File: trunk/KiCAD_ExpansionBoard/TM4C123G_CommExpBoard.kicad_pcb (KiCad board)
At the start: 2 copper layers, 50.8 x 58.4 mm, 58 parts, among them J1 TI_BOOSTER_40_J1, J2 TI_BOOSTER_40_J2, J3 TI_BOOSTER_40_J3, J4 TI_BOOSTER_40_J4, P1 ANT_GND, P10 EB_GPIO0, P5 ANT_C, P6 CAN, P7 UART1, P8 RS485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

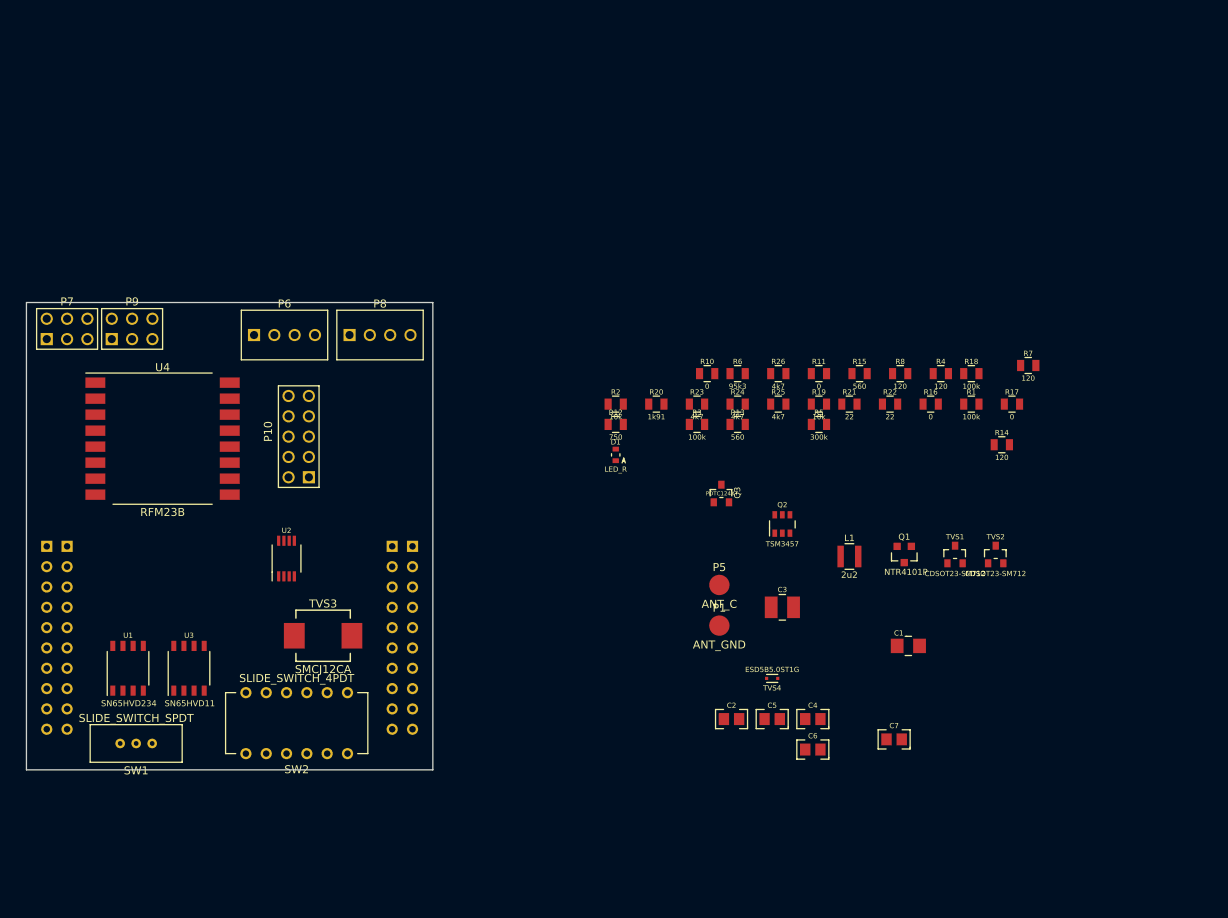
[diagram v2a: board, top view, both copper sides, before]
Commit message: Eliminata R8 e collegata la piazzola P1 direttamente al pin 2 del RFM23B. Schema elettrico alla versione 0.3.3 Cretata la BOM definitiva in (TM4C123G_CommExpBoard_BOM.xlsx e TM4C123G_CommExpBoard.csv) Completato lo sbroglio del PCB con serigrafie posizionate complete di logo OHSW. PCB alla versione 0.2
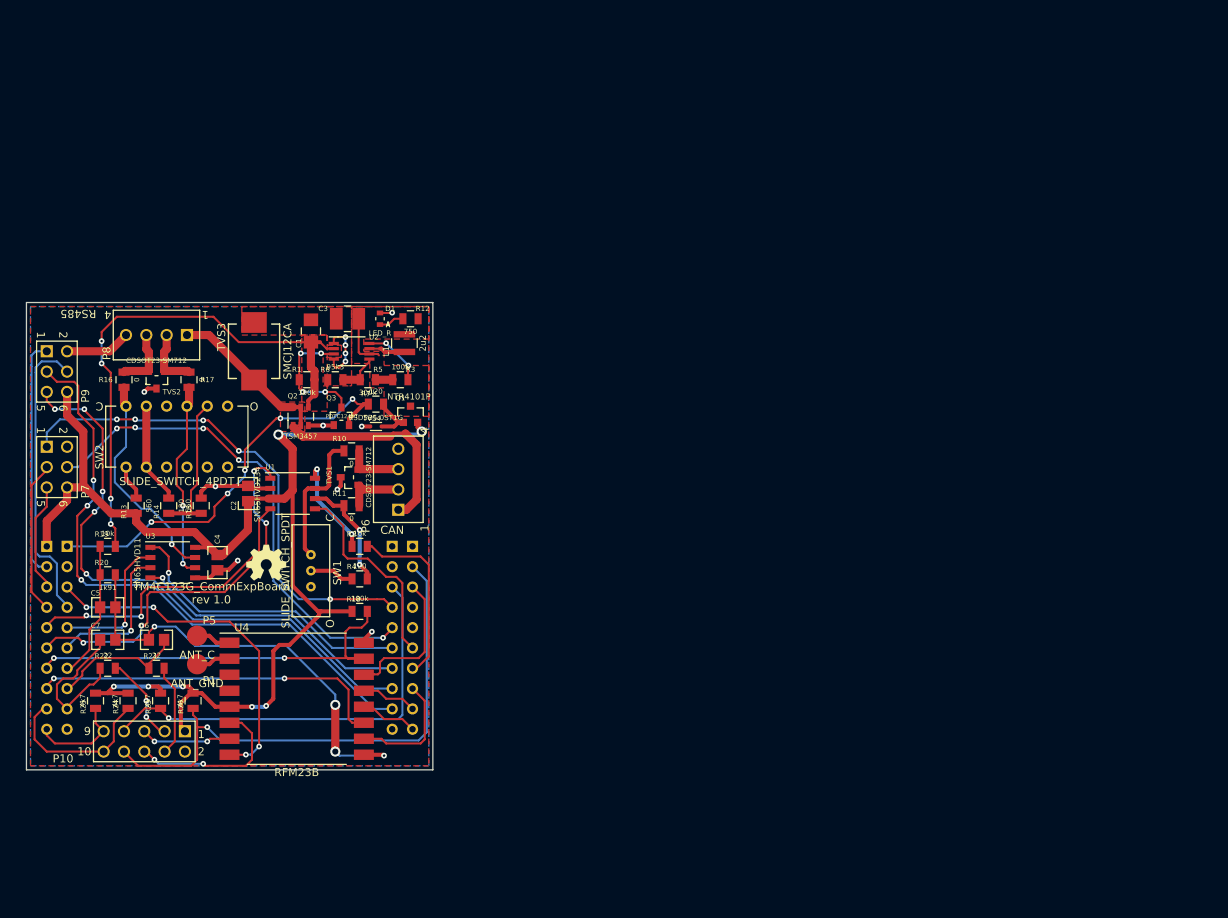
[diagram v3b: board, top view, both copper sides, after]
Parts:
- removed R8: 120, R_0805_MD
- added G1: LOGO, LOGO, F.Cu at (155.7, 89.7)
- moved TVS2 107.2 mm to (142.0, 66.8), turned to 180 degrees
- moved R14 104.4 mm to (143.5, 82.5), turned to 90 degrees
- moved R22 103.2 mm to (135.9, 102.9), turned to 180 degrees
- moved R17 102.9 mm to (146.1, 66.8), turned to 90 degrees
- moved R16 100.9 mm to (137.9, 66.8), turned to 90 degrees
- moved C7 99.1 mm to (135.9, 99.3), turned to 180 degrees
- moved R25 93.1 mm to (134.4, 106.9), turned to 270 degrees
- moved R21 92.7 mm to (142.0, 102.9), turned to 180 degrees
- moved R19 90.7 mm to (135.9, 87.6), turned to 180 degrees
- moved R24 84.7 mm to (138.4, 106.9), turned to 270 degrees
- moved C1 84.4 mm to (161.3, 60.7), turned to 270 degrees
- moved C5 84.2 mm to (135.9, 95.2), turned to 180 degrees
- moved R15 83.9 mm to (147.6, 82.5), turned to 270 degrees
- moved R26 83.8 mm to (146.6, 106.9), turned to 270 degrees
- moved C6 83.2 mm to (142.0, 99.3)
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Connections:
- C1 pad 1: N-0000073 (its old number) -> +12V_BUS
- J3 pad 1: (no net) -> +5V_TLP
- P1 pad 1: GND -> N-0000053
- P6 pad 2: /Expansion Board/CAN_H -> /Expansion Board/CAN_L
- P6 pad 3: /Expansion Board/CAN_L -> /Expansion Board/CAN_H
- Q1 pad G: N-0000064 (its old number) -> N-0000069
- Q2 pad S: (no net) -> +12V_BUS
- Q3 pad 2: (no net) -> +5V_TLP
- R1 pad 2: N-0000073 (its old number) -> +12V_BUS
- R19 pad 1: (no net) -> +12V_BUS
- R7 pad 1: N-0000076 -> N-0000069
- R7 pad 2: (no net) -> +5V_TLP
- TVS4 pad 2: N-0000076 -> N-0000069
- U2 pad 2: N-0000073 (its old number) -> +12V_BUS
- U4 pad 2: GND -> N-0000053
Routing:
- net +3.3V: track 0.00 -> 159.3 mm, vias 0 -> 7
- net GND: track 0.00 -> 97.6 mm, vias 0 -> 16
- net /TM4C123G Connectors/UART2_TX: track 0.00 -> 76.3 mm, vias 0 -> 3
- net /TM4C123G Connectors/UART2_RX: track 0.00 -> 73.3 mm, vias 0 -> 5
- net /TM4C123G Connectors/I2C0_SCL: track 0.00 -> 68.1 mm, vias 0 -> 1
- net +12V_BUS: track 0.00 -> 67.6 mm, vias 0 -> 4
- net /TM4C123G Connectors/UART1_RTS: track 0.00 -> 63.0 mm, vias 0 -> 5
- net /TM4C123G Connectors/UART1_CTS: track 0.00 -> 61.7 mm, vias 0 -> 5
- net /TM4C123G Connectors/I2C0_SDA: track 0.00 -> 53.5 mm, vias 0 -> 1
- net +5V_TLP: track 0.00 -> 52.1 mm, vias 0 -> 5
- net /Expansion Board/RFM_SDN: track 0.00 -> 50.5 mm, vias 0 -> 2
- net /Expansion Board/CAN0_TX: track 0.00 -> 49.5 mm, vias 0 -> 4
- net /TM4C123G Connectors/+12V_BUS_UNP: track 0.00 -> 47.9 mm
- net /Expansion Board/RFM_MOSI: track 0.00 -> 44.8 mm, vias 0 -> 2
- net /Expansion Board/RFM_CLK: track 0.00 -> 43.5 mm, vias 0 -> 4
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- added copper zone on F.Cu, net +12V_BUS
- added copper zone on F.Cu, net +3.3V
- added copper zone on F.Cu, net /TM4C123G Connectors/+12V_BUS_UNP
- added copper zone on B.Cu, net GND
- added copper zone on F.Cu, net GND
- added copper zone on F.Cu, net N-0000063
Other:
- net class 20/20 added: clearance 0.508, trace_width 0.508, via_dia 0.9144, via_drill 0.508
- net class Default: via_dia 0.889 -> 0.7112; via_drill 0.635 -> 0.3048
- rule via_min_drill: 0.508 -> 0.2032
- rule via_min_size: 0.889 -> 0.508
- board text added: "1"
- board text added: "10"
- board text added: "2"
- board text added: "4"
- board text added: "5"
- board text added: "6"
- board text added: "9"
- board text added: "C"
- board text added: "CAN"
- board text added: "O"
- board text added: "RS485"
- board text added: "TM4C123G_CommExpBoard rev 1.0"

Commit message: Cambiato logo OSHW con il logo TI lauchpad
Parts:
- moved G1 0.92 mm to (154.9, 89.2)

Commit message: Aggiornamento revisione su serigrafia scheda (0.3 invece di 1.0). La revisione della scheda sarà la stessa del file .pcbnew
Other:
- board text added: "PWR"
- board text added: "TM4C123G_CommExpBoard Rev 0.3"
- board text removed: "TM4C123G_CommExpBoard rev 1.0"
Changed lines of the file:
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@@
     (links 139)
     (no_connects 0)
-    (area 108.280288 56.018 177.495436 123.604001)
+    (area 125.649999 57.069999 176.610001 115.650001)
     (thickness 1.6)
-    (drawings 44)
+    (drawings 46)
     (tracks 716)
     (zones 0)
@@
     (visible_elements 7FFF7FFF)
     (pcbplotparams
-      (layerselection 3145728)
-      (usegerberextensions false)
-      (excludeedgelayer true)
+      (layerselection 15761409)
+      (usegerberextensions true)
+      (excludeedgelayer false)
       (linewidth 0.150000)
-      (plotframeref false)
+      (plotframeref true)
       (viasonmask false)
       (mode 1)
@@
       (psa4output false)
       (plotreference true)
-      (plotvalue true)
+      (plotvalue false)
       (plotothertext true)
       (plotinvisibletext false)
       (padsonsilk false)
       (subtractmaskfromsilk false)
-      (outputformat 5)
+      (outputformat 1)
       (mirror false)
       (drillshape 0)
       (scaleselection 1)
-      (outputdirectory ../../../../../Desktop/))
+      (outputdirectory "../../../../../Desktop/prova gerber/"))
   )
   (net 0 "")
@@
     (at 166.37 63.246 270)
     (attr smd)
-    (fp_text reference U2 (at -1.778 -2.794 360) (layer F.SilkS)
+    (fp_text reference U2 (at -2.032 -2.54 360) (layer F.SilkS)
       (effects (font (size 0.65 0.65) (thickness 0.16)))
     )
@@
     )
   )
-  (gr_text "TM4C123G_CommExpBoard \nrev 1.0" (at 148.844 93.472) (layer F.SilkS)
+  (target plus (at 125.73 115.57) (size 0.005) (width 0.16) (layer Edge.Cuts))
+  (gr_text PWR (at 168.656 59.182 90) (layer F.SilkS)
+    (effects (font (size 0.762 0.762) (thickness 0.15875)))
+  )
+  (gr_text "TM4C123G_CommExpBoard \nRev 0.3" (at 148.844 93.472) (layer F.SilkS)
     (effects (font (size 1.016 1.016) (thickness 0.15875)))
   )

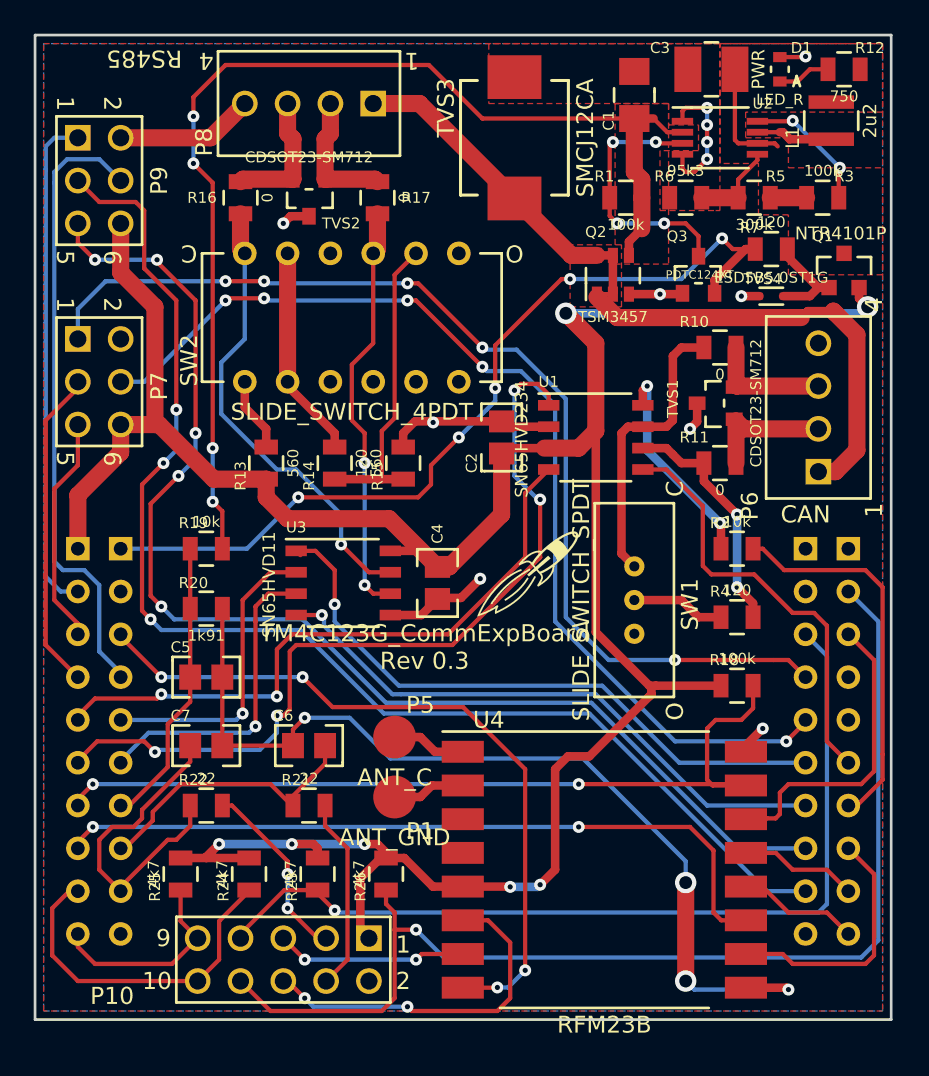
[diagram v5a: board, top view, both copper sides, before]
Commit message: Modificato il nome di P10 GPIO0 al posto di EB_GPIO0 e schematico rinominato in rev.0.3.4; di conseguenza è stato rinominato il valore di P10 anche sul PCB. Aggiornate le serigrafie dei connettori sul PCB. Aggiornato il nome della rev. sul PCB alla rev 0.4
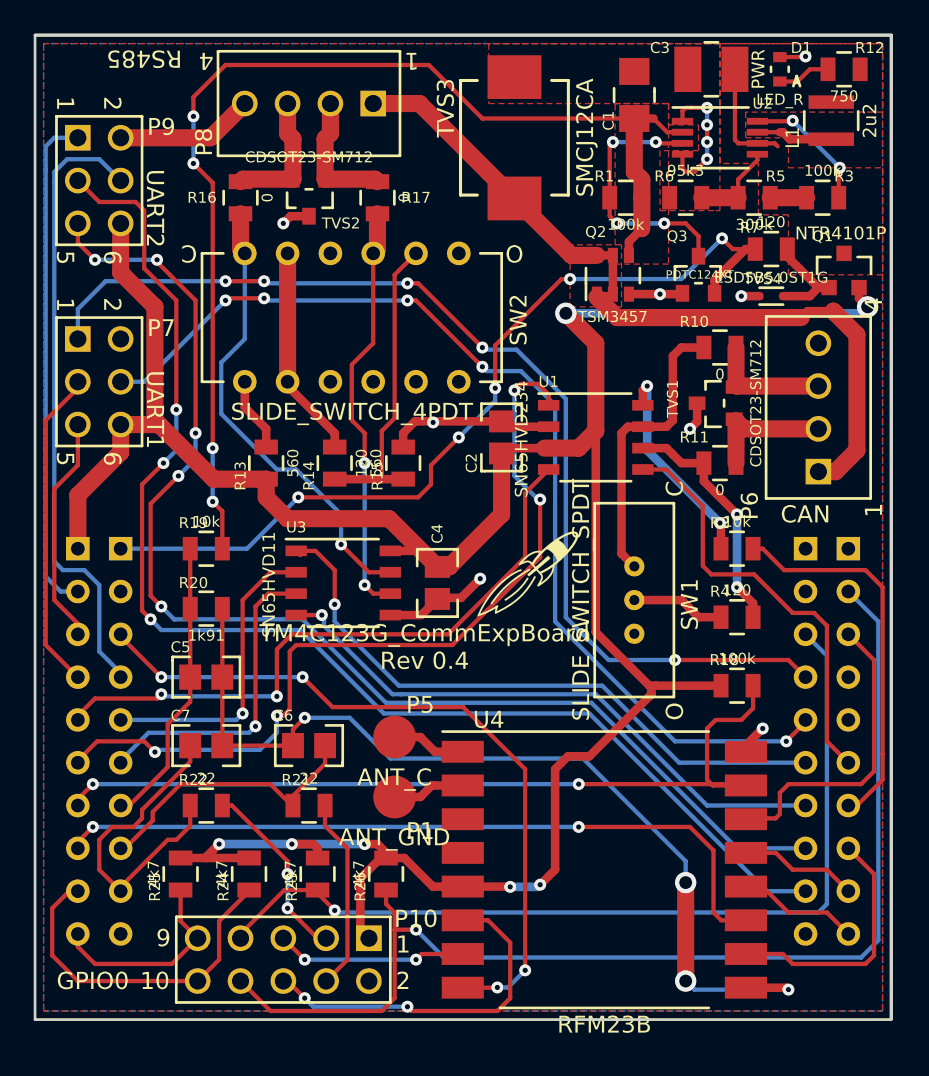
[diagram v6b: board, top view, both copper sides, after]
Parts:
- P10: value EB_GPIO0 -> GPIO0
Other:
- board text added: "GPIO0"
- board text added: "TM4C123G_CommExpBoard Rev 0.4"
- board text added: "UART1"
- board text added: "UART2"
- board text removed: "TM4C123G_CommExpBoard Rev 0.3"
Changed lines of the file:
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@@
     (links 139)
     (no_connects 0)
-    (area 125.649999 57.069999 176.610001 115.650001)
+    (area 108.280288 51.989999 181.690001 123.604001)
     (thickness 1.6)
-    (drawings 46)
+    (drawings 57)
     (tracks 716)
     (zones 0)
@@
   (title_block
     (title "TM4C123G Communication Expansion Board")
-    (rev 0.3)
+    (rev 0.4)
     (company "Luca Buccolini, Student @ Università Politecnica delle Marche")
     (comment 1 "Expansion Board for the Texas Instruments TM4C123G Launchpad ")
@@
   (layers
     (15 F.Cu signal)
-    (0 B.Cu signal)
+    (0 B.Cu signal hide)
     (16 B.Adhes user)
     (17 F.Adhes user)
@@
     (visible_elements 7FFF7FFF)
     (pcbplotparams
-      (layerselection 15761409)
+      (layerselection 299925505)
       (usegerberextensions true)
       (excludeedgelayer false)
@@
     (descr "Double rangee de contacts 2 x 4 pins")
     (tags CONN)
-    (fp_text reference P9 (at 0 -3.556 270) (layer F.SilkS)
+    (fp_text reference P9 (at -3.175 -3.683 360) (layer F.SilkS)
       (effects (font (size 1 1) (thickness 0.16)))
     )
@@
     (descr "Double rangee de contacts 2 x 4 pins")
     (tags CONN)
-    (fp_text reference P7 (at 0.254 -3.556 270) (layer F.SilkS)
+    (fp_text reference P7 (at -3.175 -3.683 360) (layer F.SilkS)
       (effects (font (size 1 1) (thickness 0.16)))
     )
@@
     (descr "Double rangee de contacts 2 x 5 pins")
     (tags CONN)
-    (fp_text reference P10 (at 10.16 -2.159 180) (layer F.SilkS)
+    (fp_text reference P10 (at -7.874 2.413 180) (layer F.SilkS)
       (effects (font (size 1.016 1.016) (thickness 0.2032)))
     )
-    (fp_text value EB_GPIO0 (at 0 -3.81 180) (layer F.SilkS) hide
+    (fp_text value GPIO0 (at 0 -3.81 180) (layer F.SilkS) hide
       (effects (font (size 1.016 1.016) (thickness 0.2032)))
     )
@@
   (module 4PDT_SLIDE_SW_MD (layer F.Cu)
     (at 144.526 73.914 180)
-    (fp_text reference SW2 (at 9.652 -2.54 270) (layer F.SilkS)
+    (fp_text reference SW2 (at -9.906 -0.127 270) (layer F.SilkS)
       (effects (font (size 1 1) (thickness 0.16)))
     )
@@
     )
   )
+  (gr_text 10 (at 132.842 113.284) (layer F.SilkS)
+    (effects (font (size 1.016 1.016) (thickness 0.15875)))
+  )
+  (gr_text GPIO0 (at 129.159 113.284) (layer F.SilkS)
+    (effects (font (size 1.016 1.016) (thickness 0.15875)))
+  )
+  (gr_text UART2 (at 132.842 67.437 270) (layer F.SilkS)
+    (effects (font (size 1.016 1.016) (thickness 0.15875)))
+  )
+  (gr_text UART1 (at 132.842 79.375 270) (layer F.SilkS)
+    (effects (font (size 1.016 1.016) (thickness 0.15875)))
+  )
+  (gr_line (start 176.53 54.61) (end 181.61 54.61) (angle 90) (layer Dwgs.User) (width 0.16))
+  (gr_line (start 179.07 52.07) (end 179.07 57.15) (angle 90) (layer Dwgs.User) (width 0.16))
+  (gr_circle (center 179.07 54.61) (end 180.594 54.61) (layer Dwgs.User) (width 0.16))
+  (gr_circle (center 179.07 118.11) (end 180.594 118.11) (layer Dwgs.User) (width 0.16))
+  (gr_line (start 176.53 118.11) (end 181.61 118.11) (angle 90) (layer Dwgs.User) (width 0.16))
+  (gr_line (start 179.07 115.57) (end 179.07 120.65) (angle 90) (layer Dwgs.User) (width 0.16))
+  (gr_line (start 123.19 52.07) (end 123.19 57.15) (angle 90) (layer Dwgs.User) (width 0.16))
+  (gr_line (start 120.65 54.61) (end 125.73 54.61) (angle 90) (layer Dwgs.User) (width 0.16))
+  (gr_circle (center 123.19 54.61) (end 124.714 54.61) (layer Dwgs.User) (width 0.16))
+  (gr_line (start 125.73 57.15) (end 176.53 57.15) (angle 90) (layer Edge.Cuts) (width 0.16))
+  (gr_line (start 176.53 57.15) (end 176.53 115.57) (angle 90) (layer Edge.Cuts) (width 0.16))
+  (target plus (at 125.73 115.57) (size 0.005) (width 0.16) (layer Edge.Cuts))
   (target plus (at 125.73 115.57) (size 0.005) (width 0.16) (layer Edge.Cuts))
   (gr_text PWR (at 168.656 59.182 90) (layer F.SilkS)
     (effects (font (size 0.762 0.762) (thickness 0.15875)))
   )
-  (gr_text "TM4C123G_CommExpBoard \nRev 0.3" (at 148.844 93.472) (layer F.SilkS)
+  (gr_text "TM4C123G_CommExpBoard \nRev 0.4" (at 148.844 93.472) (layer F.SilkS)
     (effects (font (size 1.016 1.016) (thickness 0.15875)))
   )
@@
     (effects (font (size 1.016 1.016) (thickness 0.15875)) (justify mirror))
   )
-  (gr_text 10 (at 132.969 113.284) (layer F.SilkS)
-    (effects (font (size 1.016 1.016) (thickness 0.15875)))
-  )
   (gr_text "9\n" (at 133.35 110.744) (layer F.SilkS)
     (effects (font (size 1.016 1.016) (thickness 0.15875)))
@@
     (effects (font (size 1.016 1.016) (thickness 0.15875)))
   )
-  (gr_line (start 126.238 57.658) (end 126.238 115.062) (angle 90) (layer Dwgs.User) (width 0.16))
-  (gr_line (start 176.022 57.658) (end 126.238 57.658) (angle 90) (layer Dwgs.User) (width 0.16))
-  (gr_line (start 176.022 115.062) (end 176.022 57.658) (angle 90) (layer Dwgs.User) (width 0.16))
-  (gr_line (start 126.238 115.062) (end 176.022 115.062) (angle 90) (layer Dwgs.User) (width 0.16))
   (gr_line (start 140.97 73.66) (end 140.97 76.2) (angle 90) (layer Dwgs.User) (width 0.16))
   (gr_line (start 143.51 73.66) (end 143.51 76.2) (angle 90) (layer Dwgs.User) (width 0.16))

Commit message: Schema elettrico: variate le connessione del partitore di fail-safe-biasing. R13 è di pull-down ed R15 di pull-up, quindi sono connesse rispettivamente verso gnd e +3.3V. In precedenza erano scambiate. PCB: variato il layout seguendo ciò che è stato fatto per lo schema elettrico. Risistemata la zona di rame sotto a L1 poichè in seguito alla modifica precedente, ha dato problemi (credo dovuti al cambio nome della pista).
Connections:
- R13 pad 1: +3.3V -> GND
- R15 pad 1: GND -> +3.3V
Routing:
- net +3.3V: track 159.3 -> 144.4 mm
- net GND: track 97.6 -> 103.5 mm
- net N-0000064: track 9.05 -> 12.4 mm
- net +5V_TLP: track 52.1 -> 52.8 mm
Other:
- board text added: "TM4C123G_CommExpBoard Rev 0.5"
- board text removed: "TM4C123G_CommExpBoard Rev 0.4"

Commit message: - sostituiti i pad smd dell'antenna con due pad through hole; - ridotto il numero di vias sottostanti il modulo radio RFM23B e spostati i rimanenti in maniera da evitare la sovrapposizione con i vias del modulo; - eliminate le zone di rame fra i pin dei componenti più piccoli come i resistori e condensatori 0805; - eliminati i vias vicino ai connettori "pin-header" e connesse le piste ai connettori direttamente dal lato bottom; - sostituiti i resistori di pull-up e pull-down della rete di fail-safe-bias con dei resistori di valore doppio circa (560->1k2);
Aggiunta la cartella "PCB_fabrication" che contiene:
- il file excel (BOM);
- i file per le forature;
- i file Gerber;
- alcuni file .txt che descrivono il contenuto delle rispettive cartelle.
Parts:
- R13, R15: value 560 -> 1k2
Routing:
- net N-0000069: track 12.4 -> 26.8 mm
- net /TM4C123G Connectors/I2C0_SDA: track 53.5 -> 57.5 mm
- net GND: track 103.5 -> 107.4 mm, vias 16 -> 17
- net +3.3V: track 144.4 -> 148.1 mm
- net /TM4C123G Connectors/I2C0_SCL: track 68.1 -> 69.8 mm
- net /Expansion Board/RFM_MOSI: track 44.8 -> 46.4 mm, vias 2 -> 1
- net /Expansion Board/RFM_SDN: track 50.5 -> 51.6 mm, vias 2 -> 1
- net /Expansion Board/RFM_CLK: track 43.5 -> 44.6 mm, vias 4 -> 3
- net /Expansion Board/RFM_GPIO0: track 21.2 -> 21.6 mm, vias 2 -> 1
- net /TM4C123G Connectors/EXT_AIN0: track 11.1 -> 10.8 mm, vias 2 -> 1
- net /Expansion Board/CAN0_RX: track 38.2 -> 38.0 mm, vias 2 -> 1
- net /TM4C123G Connectors/UART1_CTS: track 61.7 -> 61.9 mm, vias 5 -> 4
- net /TM4C123G Connectors/UART2_RX: vias 5 -> 4
- net /TM4C123G Connectors/RFM_GPIO0: vias 2 -> 1
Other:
- board text added: "TM4C123G_CommExpBoard Rev 1.0"
- board text removed: "TM4C123G_CommExpBoard Rev 0.5"
